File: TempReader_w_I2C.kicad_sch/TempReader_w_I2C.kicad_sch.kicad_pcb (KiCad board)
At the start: 4 copper layers, 40 x 47 mm, 47 parts, among them J1 NRF Pin Header, J2 BME Pin Header, J3 PowerHeader, SW1 D6R90F2LFS, U5 MIC5205-3.3YM5, Y2 16Mhz

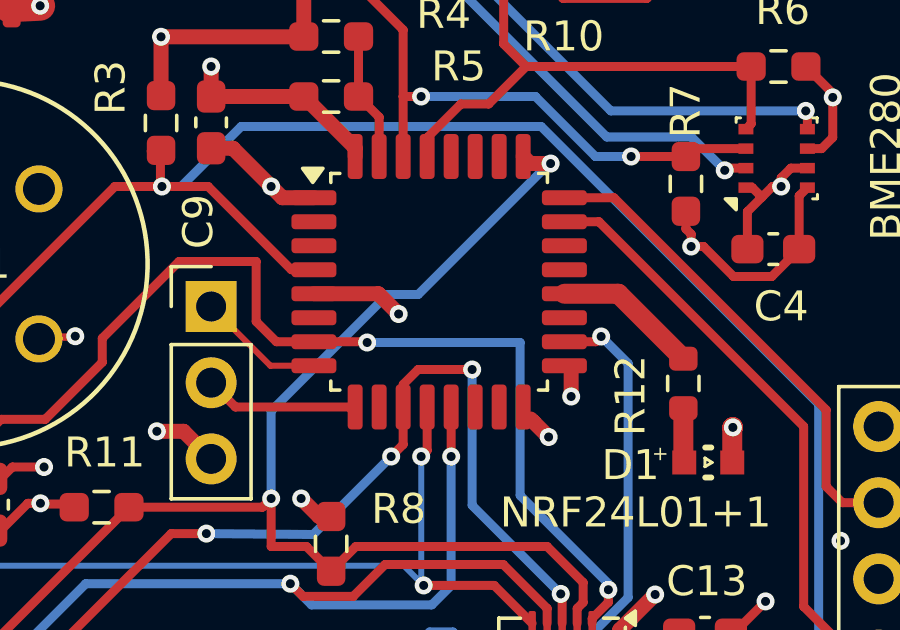
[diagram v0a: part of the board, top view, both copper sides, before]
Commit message: Change UART pins again
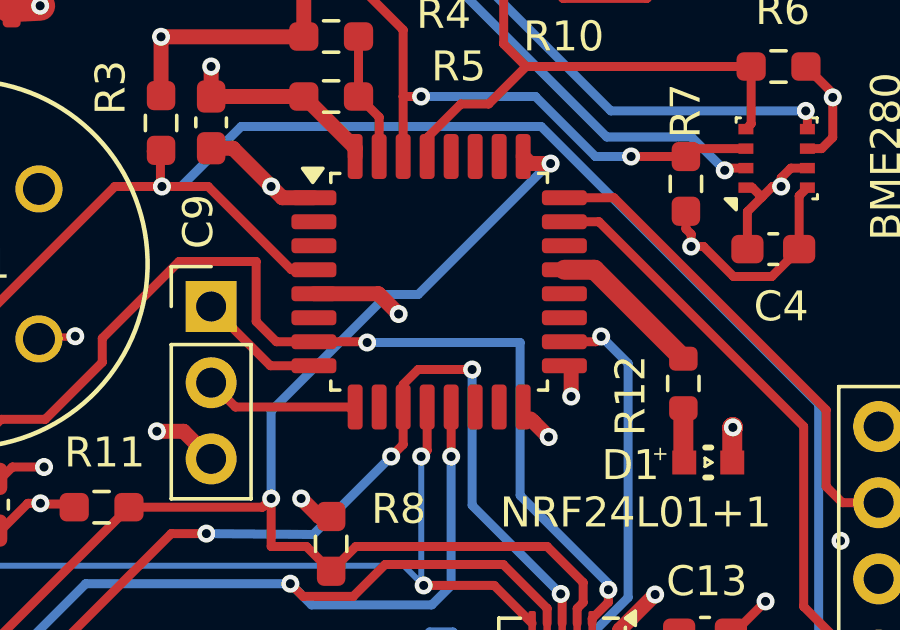
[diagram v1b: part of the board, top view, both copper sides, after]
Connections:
- R12 pad 1: Net-(STM32F030R8-PA10) -> Net-(STM32F030R8-PA11)
- STM32F030R8 pad 19: unconnected-(STM32F030R8-PA9-Pad19) -> UART_TX
- STM32F030R8 pad 20: Net-(STM32F030R8-PA10) -> UART_RX
- STM32F030R8 pad 21: unconnected-(STM32F030R8-PA11-Pad21) -> Net-(STM32F030R8-PA11)
- STM32F030R8 pad 9: UART_RX -> UART_RX(nucleo)
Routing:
- net Net-(STM32F030R8-PA11): track 0.00 -> 5.19 mm
- net Net-(STM32F030R8-PA10): track 4.86 -> 0.00 mm

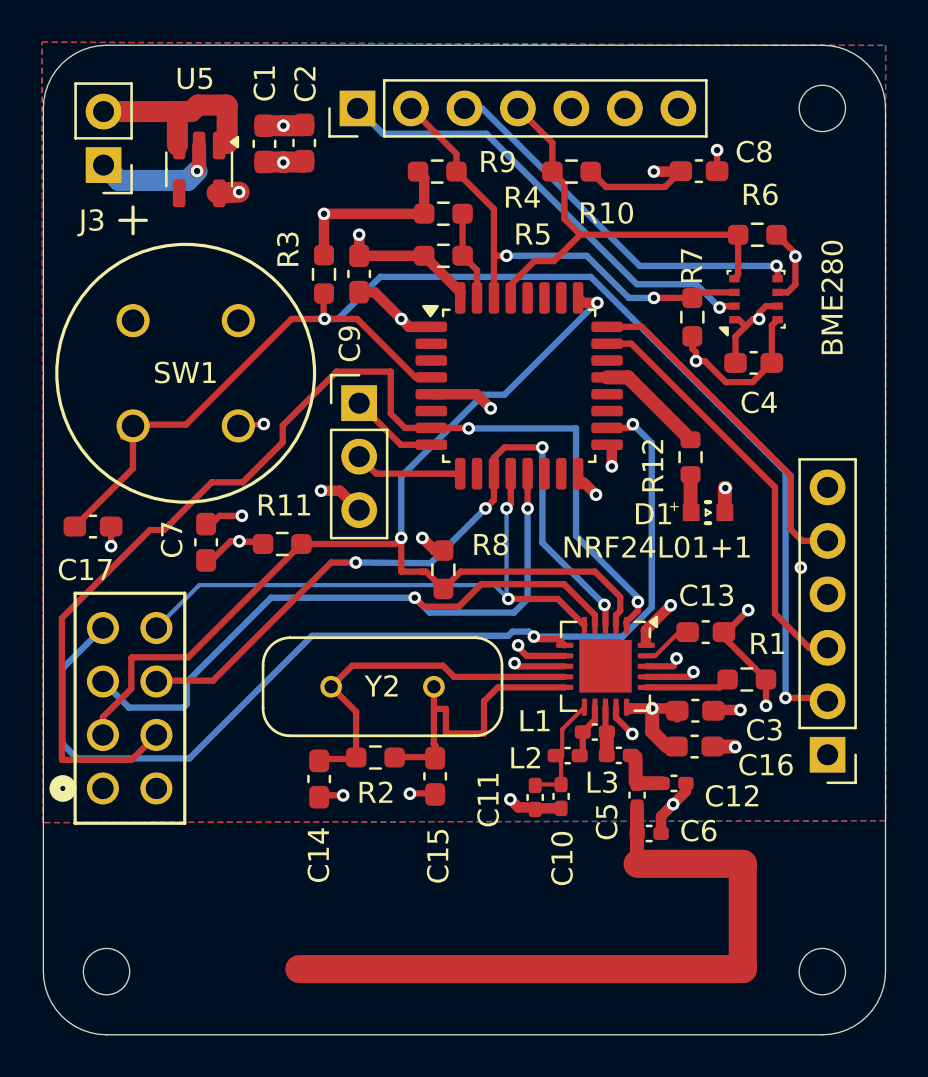
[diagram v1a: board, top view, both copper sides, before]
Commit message: Changed RAM settings in config
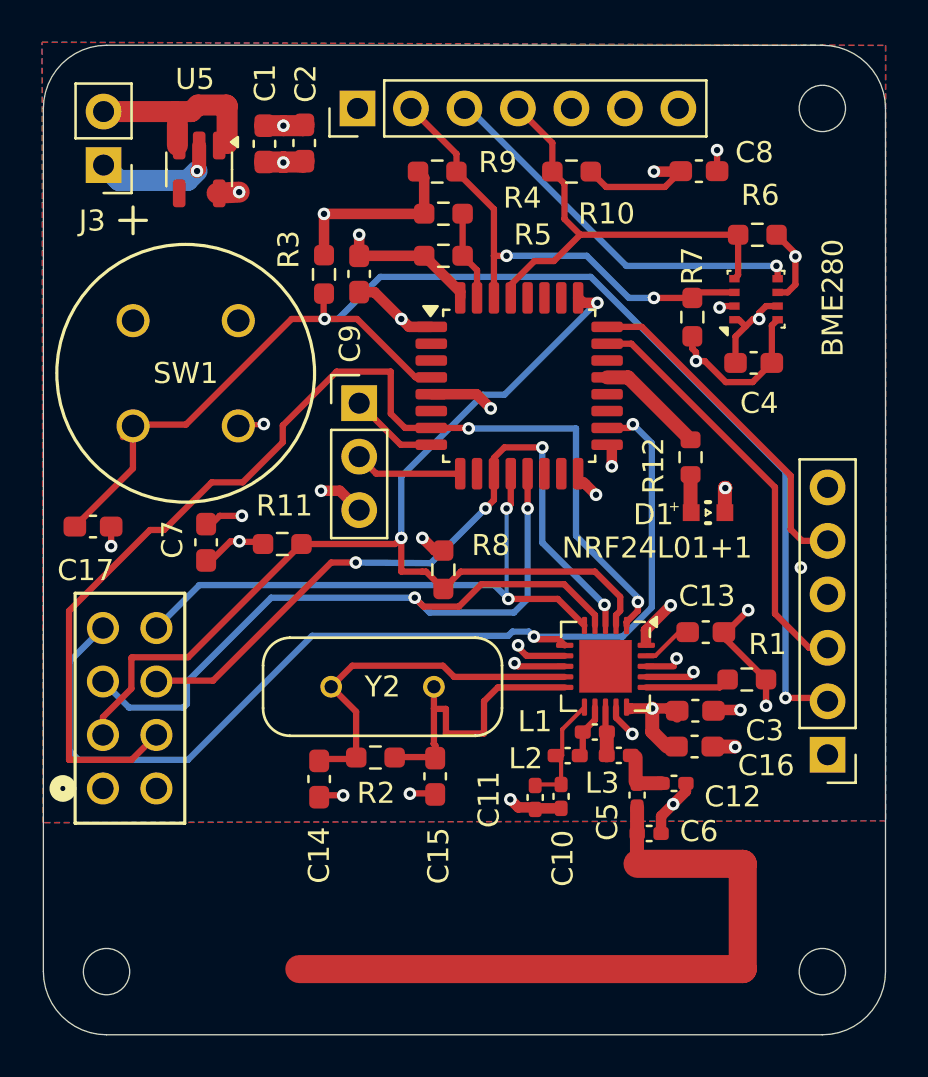
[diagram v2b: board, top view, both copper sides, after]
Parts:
- R12: value 165 -> 1000
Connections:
- BME280 pad 2: BME_CSB -> +3V3
- J2 pad 1: BME_CSB -> +3V3
- STM32F030R8 pad 19: UART_TX -> unconnected-(STM32F030R8-PA9-Pad19)
- STM32F030R8 pad 20: UART_RX -> unconnected-(STM32F030R8-PA10-Pad20)
- STM32F030R8 pad 9: UART_RX(nucleo) -> UART_RX
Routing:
- net BME_CSB: track 21.9 -> 0.00 mm, vias 1 -> 0
- net +3V3: track 52.1 -> 52.9 mm, vias 14 -> 15

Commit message: Nucleo branch created
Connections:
- BME280 pad 5: BME_SDO -> GND1
- J2 pad 3: BME_SDO -> GND1
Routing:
- net GND1: track 54.0 -> 73.1 mm, vias 24 -> 25
- net BME_SDO: track 19.1 -> 0.00 mm, vias 1 -> 0
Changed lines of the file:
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@@
 	(net 39 "unconnected-(SW1-Pad1)")
 	(net 40 "unconnected-(SW1-Pad2)")
-	(net 41 "BME_SDO")
-	(net 42 "unconnected-(J2-Pin_6-Pad6)")
-	(net 43 "Net-(D1-Pad2)")
-	(net 44 "unconnected-(STM32F030R8-PA10-Pad20)")
-	(net 45 "Net-(STM32F030R8-PA11)")
-	(net 46 "unconnected-(STM32F030R8-PA9-Pad19)")
+	(net 41 "unconnected-(J2-Pin_6-Pad6)")
+	(net 42 "Net-(D1-Pad2)")
+	(net 43 "unconnected-(STM32F030R8-PA10-Pad20)")
+	(net 44 "Net-(STM32F030R8-PA11)")
+	(net 45 "unconnected-(STM32F030R8-PA9-Pad19)")
 	(footprint "Capacitor_SMD:C_0603_1608Metric_Pad1.08x0.95mm_HandSolder"
 		(layer "F.Cu")
@@
 			(layers "F.Cu" "F.Paste" "F.Mask")
 			(roundrect_rratio 0.25)
-			(net 45 "Net-(STM32F030R8-PA11)")
+			(net 44 "Net-(STM32F030R8-PA11)")
 			(pintype "passive")
 		)
@@
 			(layers "F.Cu" "F.Paste" "F.Mask")
 			(roundrect_rratio 0.25)
-			(net 43 "Net-(D1-Pad2)")
+			(net 42 "Net-(D1-Pad2)")
 			(pintype "passive")
 		)
@@
 			(layers "*.Cu" "*.Mask")
 			(remove_unused_layers no)
-			(net 41 "BME_SDO")
+			(net 2 "GND1")
 			(pinfunction "Pin_3")
 			(pintype "passive")
@@
 			(layers "*.Cu" "*.Mask")
 			(remove_unused_layers no)
-			(net 42 "unconnected-(J2-Pin_6-Pad6)")
+			(net 41 "unconnected-(J2-Pin_6-Pad6)")
 			(pinfunction "Pin_6")
 			(pintype "passive+no_connect")
@@
 			(layers "F.Cu" "F.Paste" "F.Mask")
 			(roundrect_rratio 0.25)
-			(net 46 "unconnected-(STM32F030R8-PA9-Pad19)")
+			(net 45 "unconnected-(STM32F030R8-PA9-Pad19)")
 			(pinfunction "PA9")
 			(pintype "bidirectional+no_connect")
@@
 			(layers "F.Cu" "F.Paste" "F.Mask")
 			(roundrect_rratio 0.25)
-			(net 44 "unconnected-(STM32F030R8-PA10-Pad20)")
+			(net 43 "unconnected-(STM32F030R8-PA10-Pad20)")
 			(pinfunction "PA10")
 			(pintype "bidirectional+no_connect")
@@
 			(layers "F.Cu" "F.Paste" "F.Mask")
 			(roundrect_rratio 0.25)
-			(net 45 "Net-(STM32F030R8-PA11)")
+			(net 44 "Net-(STM32F030R8-PA11)")
 			(pinfunction "PA11")
 			(pintype "bidirectional")
@@
 			(size 0.8 0.8)
 			(layers "F.Cu" "F.Paste" "F.Mask")
-			(net 43 "Net-(D1-Pad2)")
+			(net 42 "Net-(D1-Pad2)")
 			(pintype "passive")
 			(solder_mask_margin 0.102)
@@
 			(size 0.5 0.35)
 			(layers "F.Cu" "F.Paste" "F.Mask")
-			(net 41 "BME_SDO")
+			(net 2 "GND1")
 			(pinfunction "SDO")
 			(pintype "bidirectional")
@@
 	)
 	(segment
+		(start 189.81 80.48)
+		(end 189.8 80.47)
+		(width 0.3)
+		(layer "F.Cu")
+		(net 2)
+	)
+	(segment
 		(start 187.325 98.125)
 		(end 187.325 97.875)
@@
 	)
 	(segment
+		(start 174.62 73.38)
+		(end 175 73)
+		(width 0.3)
+		(layer "F.Cu")
+		(net 2)
+	)
+	(segment
 		(start 187.39 91.03)
 		(end 187.39 91.02)
@@
 	)
 	(segment
+		(start 189.82 80.49)
+		(end 189.82 80.48)
+		(width 0.3)
+		(layer "F.Cu")
+		(net 2)
+	)
+	(segment
+		(start 189.875 81.0875)
+		(end 189.875 80.545)
+		(width 0.3)
+		(layer "F.Cu")
+		(net 2)
+	)
+	(segment
 		(start 189 83)
 		(end 189 82.7125)
@@
 	)
 	(segment
+		(start 189.875 80.545)
+		(end 189.82 80.49)
+		(width 0.3)
+		(layer "F.Cu")
+		(net 2)
+	)
+	(segment
 		(start 187.875 83.8375)
 		(end 188.35625 83.35625)
@@
 	)
 	(segment
+		(start 189.82 80.48)
+		(end 189.81 80.48)
+		(width 0.3)
+		(layer "F.Cu")
+		(net 2)
+	)
+	(segment
 		(start 185.7 100)
 		(end 185.88 99.82)
@@
 	)
 	(via
+		(at 189.82 80.48)
+		(size 0.6)
+		(drill 0.3)
+		(layers "F.Cu" "B.Cu")
+		(net 2)
+	)
+	(via
 		(at 166.4 73.82)
 		(size 0.6)
@@
 	)
 	(segment
+		(start 175.21 73)
+		(end 175 73)
+		(width 0.3)
+		(layer "B.Cu")
+		(net 2)
+	)
+	(segment
+		(start 189.82 80.48)
+		(end 182.69 80.48)
+		(width 0.3)
+		(layer "B.Cu")
+		(net 2)
+	)
+	(segment
+		(start 182.69 80.48)
+		(end 175.21 73)
+		(width 0.3)
+		(layer "B.Cu")
+		(net 2)
+	)
+	(segment
 		(start 158.59 76.42)
 		(end 157.86 75.69)
@@
 	)
 	(segment
-		(start 189.81 80.48)
-		(end 189.8 80.47)
-		(width 0.3)
-		(layer "F.Cu")
-		(net 41)
-	)
-	(segment
-		(start 174.62 73.38)
-		(end 175 73)
-		(width 0.3)
-		(layer "F.Cu")
-		(net 41)
-	)
-	(segment
-		(start 189.82 80.49)
-		(end 189.82 80.48)
-		(width 0.3)
-		(layer "F.Cu")
-		(net 41)
-	)
-	(segment
-		(start 189.875 81.0875)
-		(end 189.875 80.545)
-		(width 0.3)
-		(layer "F.Cu")
-		(net 41)
-	)
-	(segment
-		(start 189.875 80.545)
-		(end 189.82 80.49)
-		(width 0.3)
-		(layer "F.Cu")
-		(net 41)
-	)
-	(segment
-		(start 189.82 80.48)
-		(end 189.81 80.48)
-		(width 0.3)
-		(layer "F.Cu")
-		(net 41)
-	)
-	(via
-		(at 189.82 80.48)
-		(size 0.6)
-		(drill 0.3)
-		(layers "F.Cu" "B.Cu")
-		(net 41)
-	)
-	(segment
-		(start 175.21 73)
-		(end 175 73)
-		(width 0.3)
-		(layer "B.Cu")
-		(net 41)
-	)
-	(segment
-		(start 189.82 80.48)
-		(end 182.69 80.48)
-		(width 0.3)
-		(layer "B.Cu")
-		(net 41)
-	)
-	(segment
-		(start 182.69 80.48)
-		(end 175.21 73)
-		(width 0.3)
-		(layer "B.Cu")
-		(net 41)
-	)
-	(segment
 		(start 185.74 92.17)
 		(end 185.77 92.2)
 		(width 0.6666)
 		(layer "F.Cu")
-		(net 43)
+		(net 42)
 	)
 	(segment
@@
 		(width 0.6666)
 		(layer "F.Cu")
-		(net 43)
+		(net 42)
 	)
 	(segment
@@
 		(width 0.6666)
 		(layer "F.Cu")
-		(net 45)
+		(net 44)
 	)
 	(segment
@@
 		(width 0.6666)
 		(layer "F.Cu")
-		(net 45)
+		(net 44)
 	)
 	(zone
